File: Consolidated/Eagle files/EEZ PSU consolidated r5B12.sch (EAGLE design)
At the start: 544 parts, among them IC1 LTC3864EMSE#PBF, IC10 DAC8552IDGKTG4, IC11 ADG465SOT-23, IC12 TS5A9411DCKT, IC13 ADS1120IPWR, IC14 LP339D, IC15 TPD4E002DRLR, IC16 TPD2E001DZDR, IC17 ADUM3160BRWZ, IC18 TLC5925IDBQR, IC19 Si8641EC-B-IS1, IC2 LP2951SO8, IC20 SI8651EC-B-IS1, IC21 SI8651EC-B-IS1, IC22 LD1117ADT33TR, IC23 Si8641EC-B-IS1, IC24 PCA21125T/Q900/1,1, IC25 AT25256B-SSHL-B, IC26 W5500, IC27 BC857BS, IC28 TLC555, IC29 SN74LVC08APWR, IC3 TL783CKTTR, IC30 SN74LV1T34DBVR, IC31 TPS3705-33D, IC32 SN74LVC2G02DCTR, IC33 74LVC1G125GW.125, IC34 TPA6205A1DGN, IC4 LTC3260EMSE#PBF, IC5 TL072D, IC6 TL072D, IC7 LTC2050HVCS8#PBF, IC8 MCP23S17-E/SS, IC9 REF5025AIDG4, J1 BS-244DSM-R, J2 1-726388-2, J3 BS-244DSM-G, J4 BS-244DSM-B, J5 BS-244DSM-R, J6 BS-244DSM-B, J7 693072010801, Q1 IRFR5305, Q10 MMBT5401, Q11 MMBT5551, Q12 MMBT5551, Q13 IRLL2705PBF, Q14 IRFR48ZPBF, Q15 IRLML2246TRPBF, Q16 2N7002, Q17 MMBT5551, Q18 MMBT5401, Q19 MMBT5551, Q2 MMBT5401, Q20 MMBT5551, Q21 BTA26-600, Q22 BTA26-600, Q23 IRLL2705PBF, Q24 2N7002, Q25 2N7002, Q26 IRLML2246TRPBF, Q27 IRLML2246TRPBF, Q28 IRLML2246TRPBF, Q29 IRLML2246TRPBF, Q3 2N7002, Q30 2N7002, Q31 IRLML2246TRPBF, Q32 2N7002, Q33 2N7002, Q4 IRFP250N, Q5 BC857C, Q6 BCP56-16.115, Q7 IRFR5305, Q8 BCP56-16.115, Q9 MMBT5401, SW1 A101SYCQ04, SW2 PEC12R-4225F-S0024, SW3 1301.9316, X1 39-30-1039, X10 826629-5, X11 2411-01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

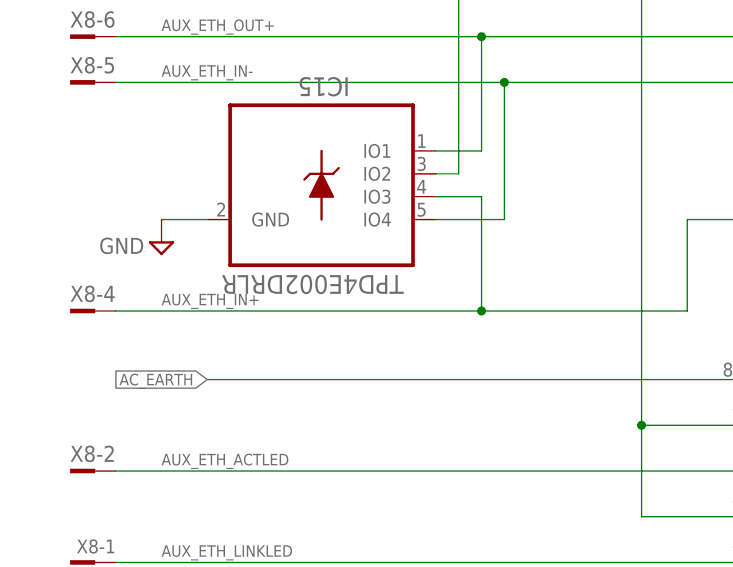
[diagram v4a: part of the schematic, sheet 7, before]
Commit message: IC15 package, wire harness update
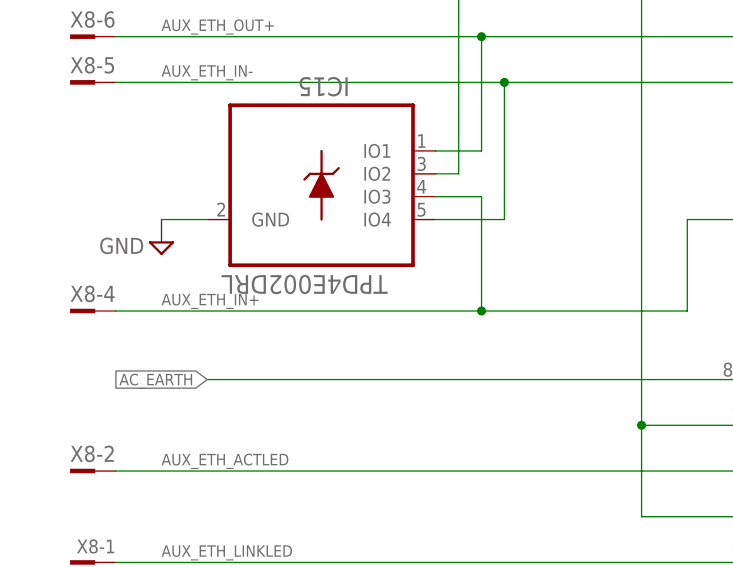
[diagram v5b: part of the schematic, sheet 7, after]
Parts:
- IC15: value TPD4E002DRLR -> TPD4E002DRL; device EEZ_Lib1:TPD4E002DRLR -> EEZ_Lib1:TPD4E002DRL
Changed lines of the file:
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@@
 <part name="FRAME6" library="frames" deviceset="DINA4_L" device=""/>
 <part name="C78" library="EEZ_Lib1" deviceset="ECAP" device="PANASONIC_H" value="220u"/>
-<part name="IC15" library="EEZ_Lib1" deviceset="TPD4E002" device="DRLR"/>
+<part name="IC15" library="EEZ_Lib1" deviceset="TPD4E002" device="DRL"/>
 <part name="IC16" library="EEZ_Lib1" deviceset="TPD2E001" device="DZDR"/>
 <part name="SUPPLY48" library="supply2" deviceset="GND" device=""/>
